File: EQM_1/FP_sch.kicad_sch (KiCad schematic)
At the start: 0 parts

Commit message: Esquema finalizado
El esquema está finalizado a falta de la asociación de footprints y la selección de valores para los pasivos
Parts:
- added C401, C402, C403, C404, C405, C406: C, symbol Device:C
- added D401, D402: LED_Filled, symbol Device:LED_Filled
- added J401, J403: Conn_Coaxial, symbol Connector:Conn_Coaxial
- added J402, J404: Screw_Terminal_01x02, symbol Connector:Screw_Terminal_01x02
- added J405, J406: ~, symbol Cmisc:Jumper_3
- added J407: Screw_Terminal_01x03, symbol Connector:Screw_Terminal_01x03
- added R401, R402, R403, R404, R405, R406, R407, R408, R409, R410, R411, R412: R, symbol Device:R
- added SW401, SW402: SW_Push, symbol Switch:SW_Push
- added TP303 (x2): TestPoint_Flag, symbol Connector:TestPoint_Flag
- added U401: CD4066BM, Package_SO:SO-14_3.9x8.65mm_P1.27mm, symbol Analog_Switch:CD4066BM
- added U402: TL082, symbol Amplifier_Operational:TL082
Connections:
- new net: R405.2, R406.2, U401.8
- new net: D401.2 (A), R409.2
- new net: R403.1, R404.1, U401.3
- new net: R407.2, R408.2, U401.11
- new net: R401.1, R402.1, U401.2
- new net: D402.2 (A), R410.2
- new net #VSS: C404.2, U402.4 (V-)
- new net +5V: C403.1, SW401.2, SW402.2, U401.14 (V_{DD})
- new net CS_{1}: J405.2, J407.1 (Pin_1)
- new net CS_{2}: J406.2, J407.2 (Pin_2)
- new net GND: C402.2, C403.2, C404.1, C405.2, C406.2, D401.1 (K), D402.1 (K), J401.2 (Ext), J402.2 (Pin_2), J403.2 (Ext), J404.2 (Pin_2), J407.3 (Pin_3), R411.2, R412.2, U401.7 (V_{SS}), U402.3 (+)
- new net SW_{1}: C405.1, J405.3, R411.1, SW401.1
- new net SW_{2}: C406.1, J406.3, R412.1, SW402.1
- new net Sig_{IN-Buff}: R405.1, R406.1, R407.1, R408.1, U402.6 (-), U402.7
- new net Sig_{IN}: J401.1 (In), J402.1 (Pin_1), TP303.1, U402.5 (+)
- new net Sig_{Out}: C401.2, J403.1 (In), J404.1 (Pin_1), R401.2, R402.2, R403.2, R404.2, TP303.1, U402.1
- new net V-: C401.1, U401.1, U401.10, U401.4, U401.9, U402.2 (-)
- new net VCC: C402.1, U402.8 (V+)
- new net V_{Control-1}: J405.1, R410.1, U401.13, U401.6
- new net V_{Control-2}: J406.1, R409.1, U401.12, U401.5
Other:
- note added: "Condensadores de bypass"
- note added: "Entrada de señal"
- note added: "Filtro programable"
- note added: "Salida de señal"
- note added: "Señales de control"

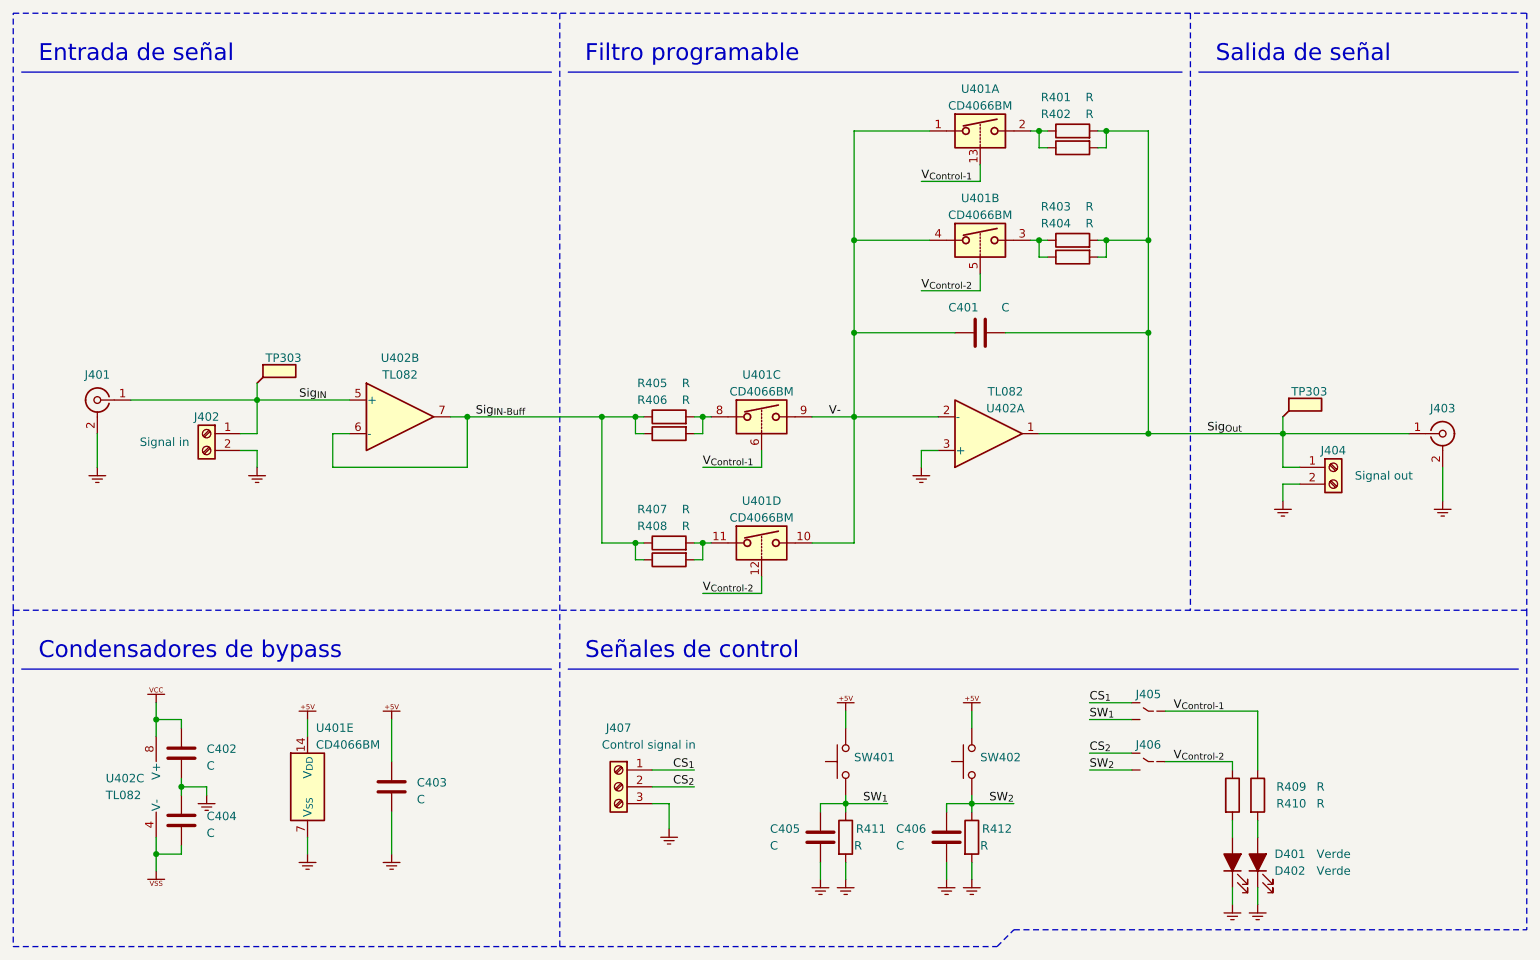
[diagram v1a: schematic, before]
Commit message: PCB-1
Primer posicionamiento de los componentes en la pcb y ligeros cambios en el esquemático.
Posicionamiento MUY BASTO, simplemente para ver que los componentes caben en las dimensiones de la pcb elegida.
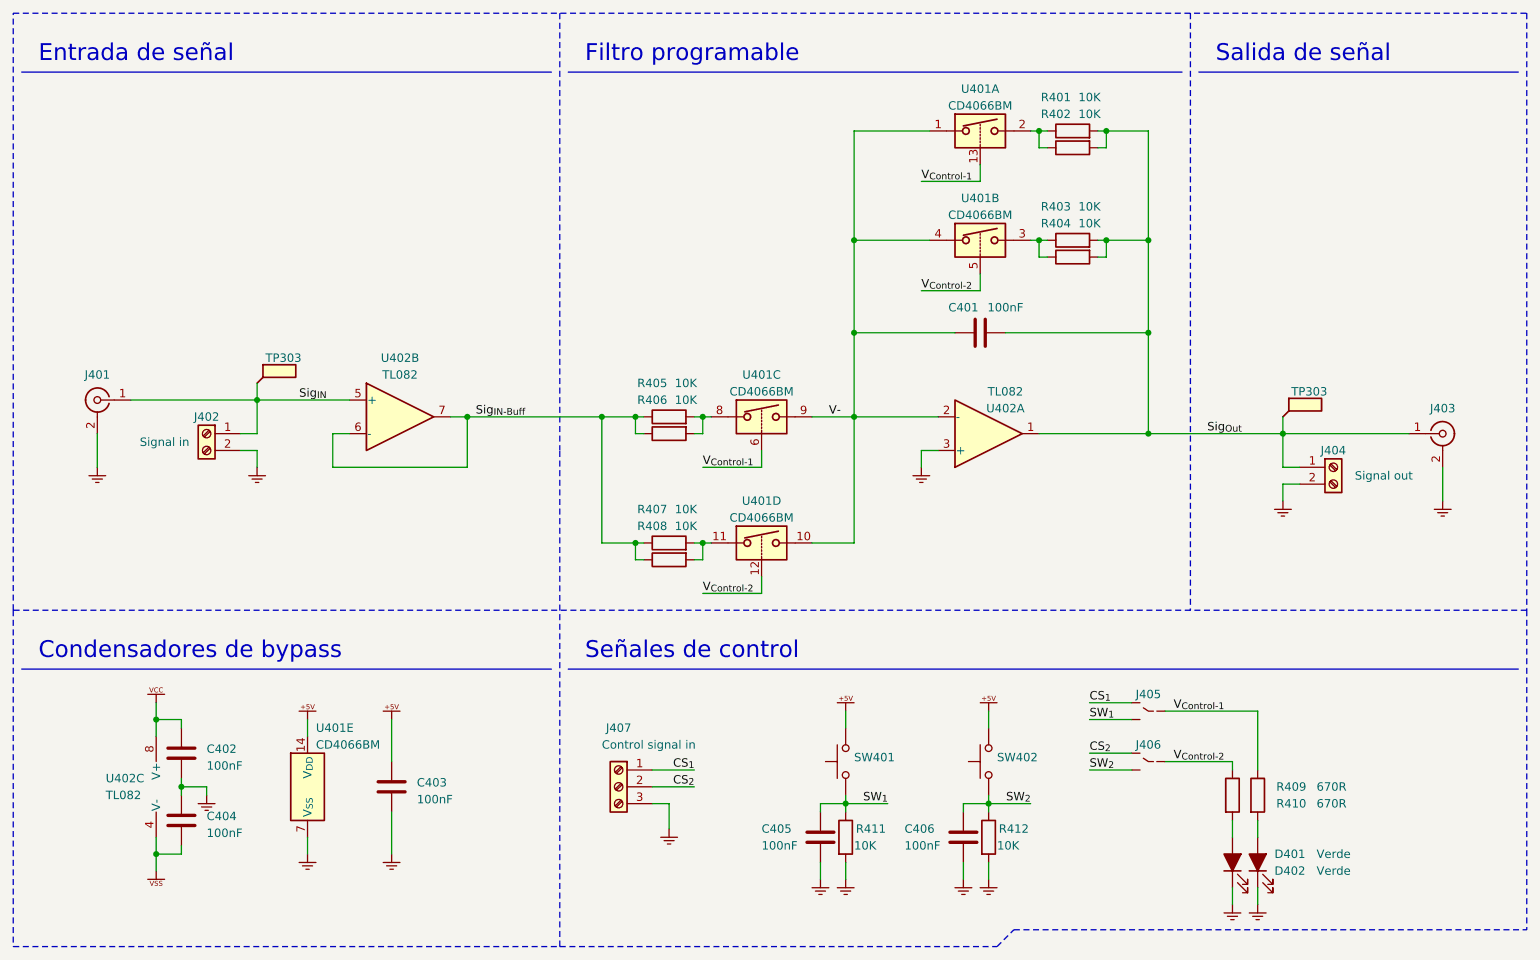
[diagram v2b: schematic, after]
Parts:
- C401, C402, C403, C404, C405, C406: value C -> 100nF; footprint (none) -> Capacitor_SMD:C_0805_2012Metric_Pad1.18x1.45mm_HandSolder
- D401, D402: footprint (none) -> Diode_SMD:D_0805_2012Metric_Pad1.15x1.40mm_HandSolder
- J401, J403: footprint (none) -> Connector_Coaxial:BNC_Amphenol_B6252HB-NPP3G-50_Horizontal
- J402, J404: footprint (none) -> TerminalBlock_Phoenix:TerminalBlock_Phoenix_MKDS-1,5-2-5.08_1x02_P5.08mm_Horizontal
- J405, J406: footprint (none) -> Connector_PinHeader_2.54mm:PinHeader_1x03_P2.54mm_Vertical
- J407: footprint (none) -> TerminalBlock_Phoenix:TerminalBlock_Phoenix_MKDS-1,5-3-5.08_1x03_P5.08mm_Horizontal
- R401, R403, R405, R407, R411, R412: value R -> 10K; footprint (none) -> Resistor_SMD:R_0805_2012Metric_Pad1.20x1.40mm_HandSolder
- R402, R404, R406, R408: value R -> 10K; footprint (none) -> Resistor_THT:R_Axial_DIN0207_L6.3mm_D2.5mm_P7.62mm_Horizontal
- R409, R410: value R -> 670R; footprint (none) -> Resistor_SMD:R_0805_2012Metric_Pad1.20x1.40mm_HandSolder
- SW401, SW402: footprint (none) -> Button_Switch_SMD:SW_Tactile_SPST_NO_Straight_CK_PTS636Sx25SMTRLFS; digikeyPN (none) -> CKN12314-2-ND; digikeyURL (none) -> https://www.digikey.com/en/products/detail/c-k/PTS636-SM50-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
- TP303: footprint (none) -> TestPoint:TestPoint_Pad_2.0x2.0mm
- U402: footprint (none) -> Package_TO_SOT_SMD:SOT-23-8
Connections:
- net CS_{1}: now also J405.1; no longer J405.2
- net CS_{2}: now also J406.1; no longer J406.2
- net V_{Control-1}: now also J405.2; no longer J405.1
- net V_{Control-2}: now also J406.2; no longer J406.1
- net #VSS renamed VSS
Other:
- moved on the sheet: C406, R412, SW402
